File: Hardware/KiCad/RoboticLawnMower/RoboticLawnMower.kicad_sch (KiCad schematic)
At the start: 7 parts, among them J10 Conn_01x02, J11 Conn_01x02

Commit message: layout update
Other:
- sheet Motor_M2 ports: added ADR_0, ADR_1, MOT_5V_OUT, MOT_ENABLE, MOT_SIGNAL, MOT_VEL, MOT_Z/F (DIR), POW_EN, SCL, SDA, ~{alert}; removed none
- sheet Motor_M3 ports: added ADR_0, ADR_1, MOT_5V_OUT, MOT_ENABLE, MOT_SIGNAL, MOT_VEL, MOT_Z/F (DIR), POW_EN, SCL, SDA, ~{alert}; removed none
- sheet Motor_M4 ports: added ADR_0, ADR_1, MOT_5V_OUT, MOT_ENABLE, MOT_SIGNAL, MOT_VEL, MOT_Z/F (DIR), POW_EN, SCL, SDA, ~{alert}; removed none
- sheet Motor_M5 ports: added ADR_0, ADR_1, MOT_5V_OUT, MOT_ENABLE, MOT_SIGNAL, MOT_VEL, MOT_Z/F (DIR), POW_EN, SCL, SDA, ~{alert}; removed none
- sheet i2c_io_pwm ports: added PWM_OUT, SCL, SDA; removed none
- sheet uC ports: added I2C_0_SCL, I2C_0_SDA, MOTOR_CONTROL, SMB_MUX_ADR_0, SMB_MUX_ADR_1, SMB_MUX_ADR_2, UART_0_RXD, UART_0_TXD; removed none

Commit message: schaltplan und layout
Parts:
- added Q1, Q2: BSS123, Package_TO_SOT_SMD:SOT-23, symbol Transistor_FET:BSS123
- added Q3, Q4: Si7141DP, Package_SO:PowerPAK_SO-8_Single, symbol Transistor_FET:Si7141DP
- added R10, R11: 100k, Resistor_SMD:R_0603_1608Metric, symbol Device:R
- added R12, R13: 1K, Resistor_SMD:R_0603_1608Metric, symbol Device:R
- added R6, R7: 100R, Resistor_SMD:R_0603_1608Metric, symbol Device:R
- added R8, R9: 1M, Resistor_SMD:R_0603_1608Metric, symbol Device:R
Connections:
- net Motor_M1/UBATT: now also Q4.5 (D); no longer J11.1 (Pin_1)
- net GNDPWR renamed GND
- net GND: now also Q1.2 (S), Q2.2 (S), R8.2, R9.2
- new net: Q2.1 (G), R7.2, R9.1
- new net: Q4.4 (G), R11.2, R13.2
- new net: Q2.3 (D), R13.1
- new net: Q3.4 (G), R10.2, R12.2
- new net: Q1.1 (G), R6.2, R8.1
- new net: Q1.3 (D), R12.1
- new net +BATT: J11.1 (Pin_1), Q3.1 (S), Q3.2 (S), Q3.3 (S), Q4.1 (S), Q4.2 (S), Q4.3 (S), R10.1, R11.1
- new net Motor_M1..4_EN: R7.1
- new net Motor_M5/UBATT: Q3.5 (D)
- new net Motor_M5_EN: R6.1
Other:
- sheet Motor_M1 ports: added none; removed POW_EN
- sheet Motor_M2 ports: added none; removed POW_EN
- sheet Motor_M3 ports: added none; removed POW_EN
- sheet Motor_M4 ports: added none; removed POW_EN
- sheet Motor_M5 ports: added none; removed POW_EN
- sheet i2c_io_pwm ports: added ~{PCA_9685_OE}; removed none
- sheet uC ports: added I2C_1_SCL, I2C_1_SDA, Motor_M1..4_EN, Motor_M5_EN, ~{PCA_9685_OE}; removed none

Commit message: Layout
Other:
- sheet i2c_smb_mux ports: added none; removed ADR_0, ADR_1, ADR_2
- sheet uC ports: added ~{SMB_MUX_RESET}; removed SMB_MUX_ADR_0, SMB_MUX_ADR_1, SMB_MUX_ADR_2
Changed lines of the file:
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@@
-    (stroke (width 0) (type default) (color 0 0 0 0))
-  )
-  (wire (pts (xy 129.54 184.15) (xy 129.54 101.6))
     (stroke (width 0) (type default) (color 0 0 0 0))
   )
@@
     (stroke (width 0) (type default) (color 0 0 0 0))
   )
+  (wire (pts (xy 139.7 196.85) (xy 130.81 196.85))
+    (stroke (width 0) (type default) (color 0 0 0 0))
+  )
   (bus (pts (xy 280.67 57.15) (xy 280.67 99.06))
     (stroke (width 0) (type default) (color 0 0 0 0))
@@
     (stroke (width 0) (type default) (color 0 0 0 0))
   )
+  (wire (pts (xy 130.81 104.14) (xy 139.7 104.14))
+    (stroke (width 0) (type default) (color 0 0 0 0))
+  )
   (wire (pts (xy 308.61 140.97) (xy 330.2 140.97))
     (stroke (width 0) (type default) (color 0 0 0 0))
@@
     (stroke (width 0) (type default) (color 0 0 0 0))
   )
-  (wire (pts (xy 129.54 101.6) (xy 139.7 101.6))
-    (stroke (width 0) (type default) (color 0 0 0 0))
-  )
   (wire (pts (xy 191.77 109.22) (xy 313.69 109.22))
     (stroke (width 0) (type default) (color 0 0 0 0))
@@
     (stroke (width 0) (type default) (color 0 0 0 0))
   )
-  (wire (pts (xy 130.81 104.14) (xy 130.81 181.61))
-    (stroke (width 0) (type default) (color 0 0 0 0))
-  )
   (wire (pts (xy 313.69 127) (xy 313.69 132.08))
     (stroke (width 0) (type default) (color 0 0 0 0))
@@
     (stroke (width 0) (type default) (color 0 0 0 0))
   )
-  (wire (pts (xy 128.27 186.69) (xy 139.7 186.69))
-    (stroke (width 0) (type default) (color 0 0 0 0))
-  )
   (wire (pts (xy 227.33 36.83) (xy 232.41 36.83))
     (stroke (width 0) (type default) (color 0 0 0 0))
@@
     (stroke (width 0) (type default) (color 0 0 0 0))
   )
+  (wire (pts (xy 130.81 196.85) (xy 130.81 104.14))
+    (stroke (width 0) (type default) (color 0 0 0 0))
+  )
   (wire (pts (xy 232.41 45.72) (xy 232.41 48.26))
     (stroke (width 0) (type default) (color 0 0 0 0))
@@
     (stroke (width 0) (type default) (color 0 0 0 0))
   )
-  (wire (pts (xy 139.7 104.14) (xy 130.81 104.14))
-    (stroke (width 0) (type default) (color 0 0 0 0))
-  )
   (wire (pts (xy 237.49 27.94) (xy 316.23 27.94))
     (stroke (width 0) (type default) (color 0 0 0 0))
@@
     (stroke (width 0) (type default) (color 0 0 0 0))
   )
-  (wire (pts (xy 130.81 181.61) (xy 139.7 181.61))
-    (stroke (width 0) (type default) (color 0 0 0 0))
-  )
   (wire (pts (xy 191.77 109.22) (xy 177.8 109.22))
     (stroke (width 0) (type default) (color 0 0 0 0))
@@
     (stroke (width 0) (type default) (color 0 0 0 0))
   )
-  (wire (pts (xy 139.7 99.06) (xy 128.27 99.06))
-    (stroke (width 0) (type default) (color 0 0 0 0))
-  )
   (wire (pts (xy 316.23 73.66) (xy 330.2 73.66))
     (stroke (width 0) (type default) (color 0 0 0 0))
@@
     (stroke (width 0) (type default) (color 0 0 0 0))
   )
-  (wire (pts (xy 128.27 99.06) (xy 128.27 186.69))
-    (stroke (width 0) (type default) (color 0 0 0 0))
-  )
   (wire (pts (xy 33.02 27.94) (xy 132.08 27.94))
     (stroke (width 0) (type default) (color 0 0 0 0))
@@
   )
   (wire (pts (xy 139.7 106.68) (xy 132.08 106.68))
-    (stroke (width 0) (type default) (color 0 0 0 0))
-  )
-  (wire (pts (xy 139.7 184.15) (xy 129.54 184.15))
     (stroke (width 0) (type default) (color 0 0 0 0))
   )
@@
       (effects (font (size 1.27 1.27)) (justify left))
     )
-    (pin "ADR_2" bidirectional (at 139.7 186.69 180)
-      (effects (font (size 1.27 1.27)) (justify left))
-    )
-    (pin "ADR_1" bidirectional (at 139.7 184.15 180)
-      (effects (font (size 1.27 1.27)) (justify left))
-    )
-    (pin "ADR_0" bidirectional (at 139.7 181.61 180)
-      (effects (font (size 1.27 1.27)) (justify left))
-    )
   )
   (sheet (at 139.7 88.9) (size 38.1 34.29) (fields_autoplaced)
@@
       (effects (font (size 1.27 1.27)) (justify right))
     )
-    (pin "SMB_MUX_ADR_0" bidirectional (at 139.7 104.14 180)
-      (effects (font (size 1.27 1.27)) (justify left))
-    )
-    (pin "SMB_MUX_ADR_1" bidirectional (at 139.7 101.6 180)
-      (effects (font (size 1.27 1.27)) (justify left))
-    )
-    (pin "SMB_MUX_ADR_2" bidirectional (at 139.7 99.06 180)
-      (effects (font (size 1.27 1.27)) (justify left))
-    )
     (pin "~{PCA_9685_OE}" bidirectional (at 177.8 111.76 0)
       (effects (font (size 1.27 1.27)) (justify right))
@@
     (pin "Motor_M5_EN" bidirectional (at 177.8 118.11 0)
       (effects (font (size 1.27 1.27)) (justify right))
+    )
+    (pin "~{SMB_MUX_RESET}" output (at 139.7 104.14 180)
+      (effects (font (size 1.27 1.27)) (justify left))
     )
   )
@@
       (reference "#PWR064") (unit 1) (value "GNDPWR") (footprint "")
     )
+    (path "/611b545d-604c-4bc1-9e50-b1bbed73205e/6ccedec2-da8e-43d4-a940-72a2030bb81b"
+      (reference "#PWR065") (unit 1) (value "+3.3V") (footprint "")
+    )
+    (path "/611b545d-604c-4bc1-9e50-b1bbed73205e/73a8e649-7fe1-4289-b359-82acac05554e"
+      (reference "#PWR066") (unit 1) (value "+3.3V") (footprint "")
+    )
+    (path "/611b545d-604c-4bc1-9e50-b1bbed73205e/d185b2e9-423d-4aa1-ad92-12e9b05fa5c3"
+      (reference "#PWR067") (unit 1) (value "GND") (footprint "")
+    )
+    (path "/611b545d-604c-4bc1-9e50-b1bbed73205e/7f40b2b2-bc40-4156-ae23-f353301d7bda"
+      (reference "#PWR068") (unit 1) (value "+3.3V") (footprint "")
+    )
+    (path "/611b545d-604c-4bc1-9e50-b1bbed73205e/323a30e9-9ec8-4d2c-8720-603c8cc6abc7"
+      (reference "#PWR069") (unit 1) (value "GND") (footprint "")
+    )
+    (path "/6306c3d8-4421-4900-a194-54ab6eebd899/eb218c4a-91a1-4e57-be43-77887926051b"
+      (reference "#PWR070") (unit 1) (value "+3.3V") (footprint "")
+    )
+    (path "/611b545d-604c-4bc1-9e50-b1bbed73205e/ea316622-f00e-479e-9b9d-83cf1784feae"
+      (reference "#PWR071") (unit 1) (value "GND") (footprint "")
+    )
     (path "/39f2b0f3-d323-43fa-8206-419714f3fe7e/66bb9d1c-8659-457d-8200-a79fe0b5ccf5"
       (reference "#PWR0101") (unit 1) (value "GNDPWR") (footprint "")
@@
       (reference "R18") (unit 1) (value "2k2") (footprint "Resistor_SMD:R_0603_1608Metric")
     )
+    (path "/611b545d-604c-4bc1-9e50-b1bbed73205e/c1ac4d05-24d2-49d1-8fd0-958c728ec42a"
+      (reference "R19") (unit 1) (value "10K") (footprint "Resistor_SMD:R_0603_1608Metric")
+    )
+    (path "/611b545d-604c-4bc1-9e50-b1bbed73205e/027d4156-3f39-45ed-96c2-fe0935c5f1bc"
+      (reference "R20") (unit 1) (value "4k7") (footprint "Resistor_SMD:R_0603_1608Metric")
+    )
+    (path "/611b545d-604c-4bc1-9e50-b1bbed73205e/743aa81b-70e2-49b2-bab9-699a75eb9c80"
+      (reference "R21") (unit 1) (value "4k7") (footprint "Resistor_SMD:R_0603_1608Metric")
+    )
+    (path "/611b545d-604c-4bc1-9e50-b1bbed73205e/ff0bdb24-c68e-4ec9-b109-7947acf76e94"
+      (reference "R22") (unit 1) (value "4k7") (footprint "Resistor_SMD:R_0603_1608Metric")
+    )
+    (path "/611b545d-604c-4bc1-9e50-b1bbed73205e/9db69c11-f599-4a53-a000-50c2575872b2"
+      (reference "R23") (unit 1) (value "4k7") (footprint "Resistor_SMD:R_0603_1608Metric")
+    )
+    (path "/611b545d-604c-4bc1-9e50-b1bbed73205e/09da38a8-d19a-4f3c-90fe-6754e1f1f7f9"
+      (reference "R24") (unit 1) (value "4k7") (footprint "Resistor_SMD:R_0603_1608Metric")
+    )
+    (path "/611b545d-604c-4bc1-9e50-b1bbed73205e/a5c8077b-77d1-402b-99fa-59909bf0cffc"
+      (reference "R25") (unit 1) (value "4k7") (footprint "Resistor_SMD:R_0603_1608Metric")
+    )
     (path "/6306c3d8-4421-4900-a194-54ab6eebd899/78684c19-73bc-4253-8b81-9d4a6248cd2f"
       (reference "R26") (unit 1) (value "47K") (footprint "Resistor_SMD:R_0603_1608Metric")
@@
       (reference "R34") (unit 1) (value "N.P.") (footprint "Resistor_SMD:R_0402_1005Metric")
     )
+    (path "/611b545d-604c-4bc1-9e50-b1bbed73205e/8a03f295-4280-476c-a74d-73323f1aa23f"
+      (reference "R35") (unit 1) (value "4k7") (footprint "Resistor_SMD:R_0603_1608Metric")
+    )
+    (path "/611b545d-604c-4bc1-9e50-b1bbed73205e/7a09fee4-0e7b-4f35-b6c2-12bd7c112439"
+      (reference "R36") (unit 1) (value "4k7") (footprint "Resistor_SMD:R_0603_1608Metric")
+    )
+    (path "/611b545d-604c-4bc1-9e50-b1bbed73205e/30251252-206f-466f-a3f4-f51e314c58c9"
+      (reference "R37") (unit 1) (value "10K") (footprint "Resistor_SMD:R_0402_1005Metric")
+    )
+    (path "/611b545d-604c-4bc1-9e50-b1bbed73205e/774526b0-09d1-48c8-9e8d-29d0938edfdc"
+      (reference "R38") (unit 1) (value "N.P.") (footprint "Resistor_SMD:R_0402_1005Metric")
+    )
+    (path "/611b545d-604c-4bc1-9e50-b1bbed73205e/0d107a27-ca60-43be-8cef-bd52e5e4e4ef"
+      (reference "R39") (unit 1) (value "10K") (footprint "Resistor_SMD:R_0402_1005Metric")
+    )
+    (path "/611b545d-604c-4bc1-9e50-b1bbed73205e/c2b299e8-c23b-47ee-b08e-a48be056f621"
+      (reference "R40") (unit 1) (value "N.P.") (footprint "Resistor_SMD:R_0402_1005Metric")
+    )
+    (path "/6306c3d8-4421-4900-a194-54ab6eebd899/4a634291-adde-4b7c-9e83-9b3ebd29c2f5"
+      (reference "R41") (unit 1) (value "4k7") (footprint "Resistor_SMD:R_0603_1608Metric")
+    )
+    (path "/6306c3d8-4421-4900-a194-54ab6eebd899/12d79ae8-cba0-4cfc-91e7-4f626e0342c8"
+      (reference "R42") (unit 1) (value "4k7") (footprint "Resistor_SMD:R_0603_1608Metric")
+    )
     (path "/39f2b0f3-d323-43fa-8206-419714f3fe7e/e02631f0-f8c8-4738-b68d-6c574a73846f"

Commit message: Layout
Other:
- sheet Motor_M1 ports: added none; removed ~{alert}
- sheet Motor_M2 ports: added none; removed ~{alert}
- sheet Motor_M3 ports: added none; removed ~{alert}
- sheet Motor_M4 ports: added none; removed ~{alert}
- sheet Motor_M5 ports: added none; removed ~{alert}
- sheet WLAN ports: added UART_RxD_uC, UART_TxD_uC; removed none
- sheet uC ports: added none; removed MOTOR_CONTROL

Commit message: LAYOUT
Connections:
- net +BATT: now also J10.1 (Pin_1)
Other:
- sheet uC ports: added MOTOR_CTR_CTN_0, MOTOR_CTR_CTN_1, MOTOR_CTR_CTN_2, MOTOR_CTR_CTN_3, MOTOR_CTR_CTN_4; removed none

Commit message: bild hinzugefügt.
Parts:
- added J16: Conn_01x06, Connector_PinHeader_2.54mm:PinHeader_1x06_P2.54mm_Vertical, symbol Connector_Generic:Conn_01x06
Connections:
- net +3.3V: now also J16.1 (Pin_1)
- net GND: now also J16.6 (Pin_6)
- new net uC/UART_0_RXD: J16.3 (Pin_3)
- new net uC/UART_0_TXD: J16.2 (Pin_2)
- new net uC/UART_0_XCK: J16.4 (Pin_4)
- new net uC/UART_0_XDIR: J16.5 (Pin_5)
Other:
- removed sheet WLAN
- sheet uC ports: added UART_0_XCK, UART_0_XDIR; removed none

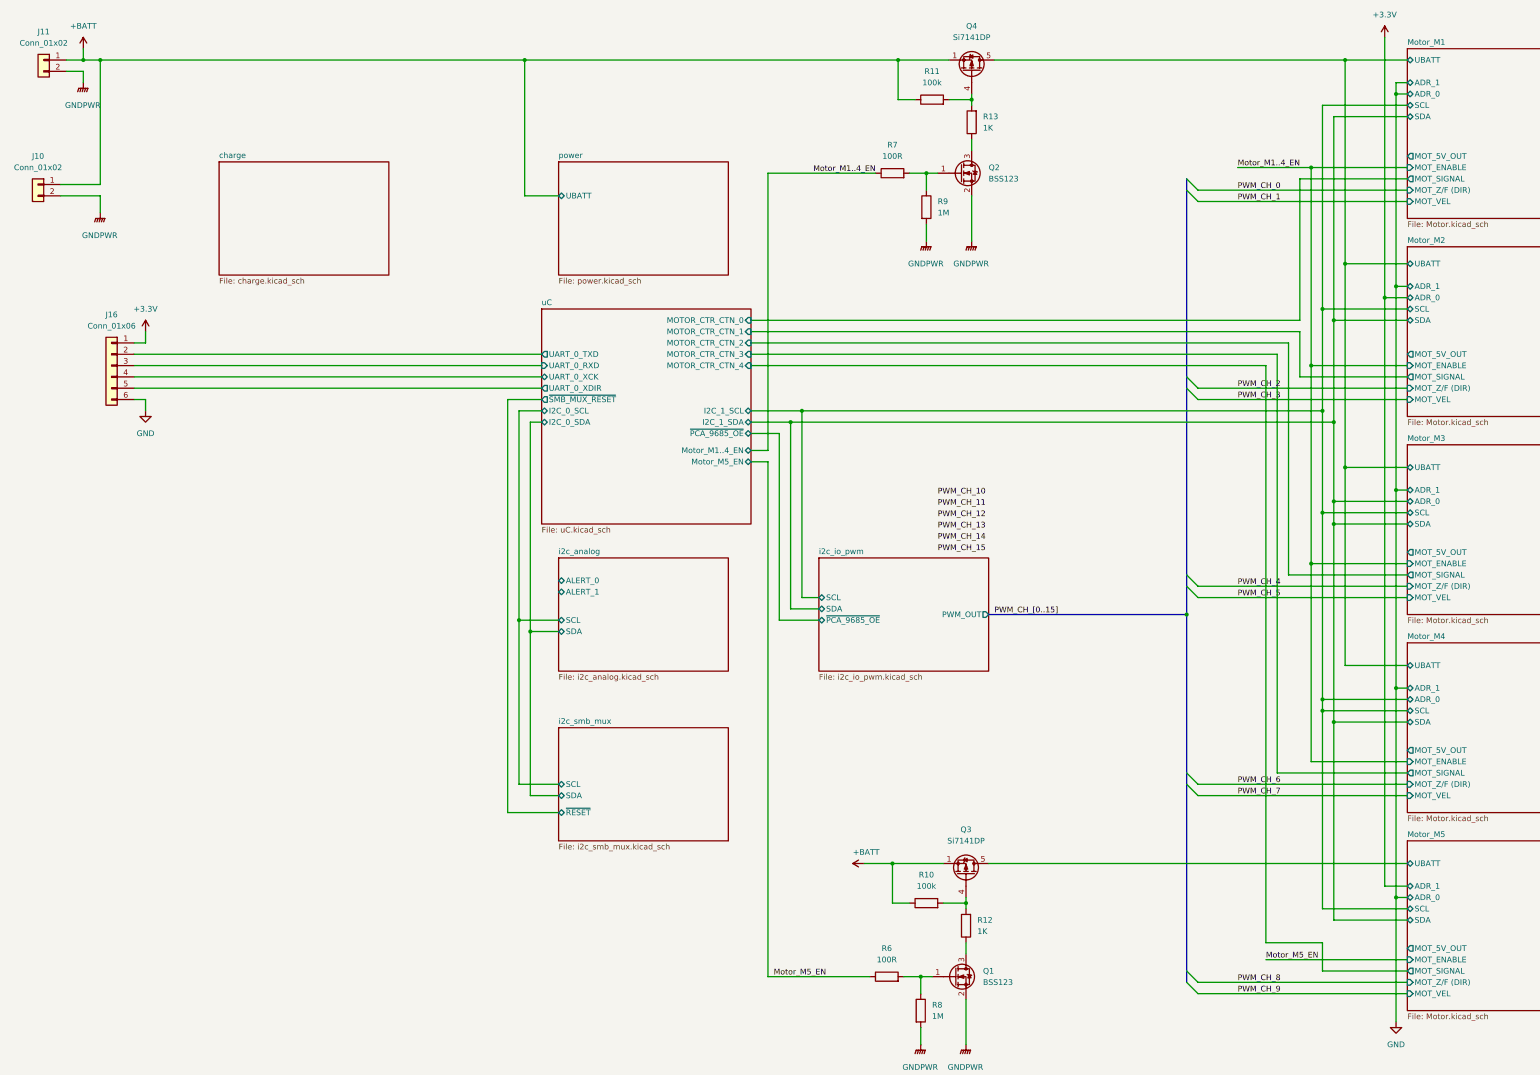
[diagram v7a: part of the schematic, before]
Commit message: Schaltplan und Layout änderung
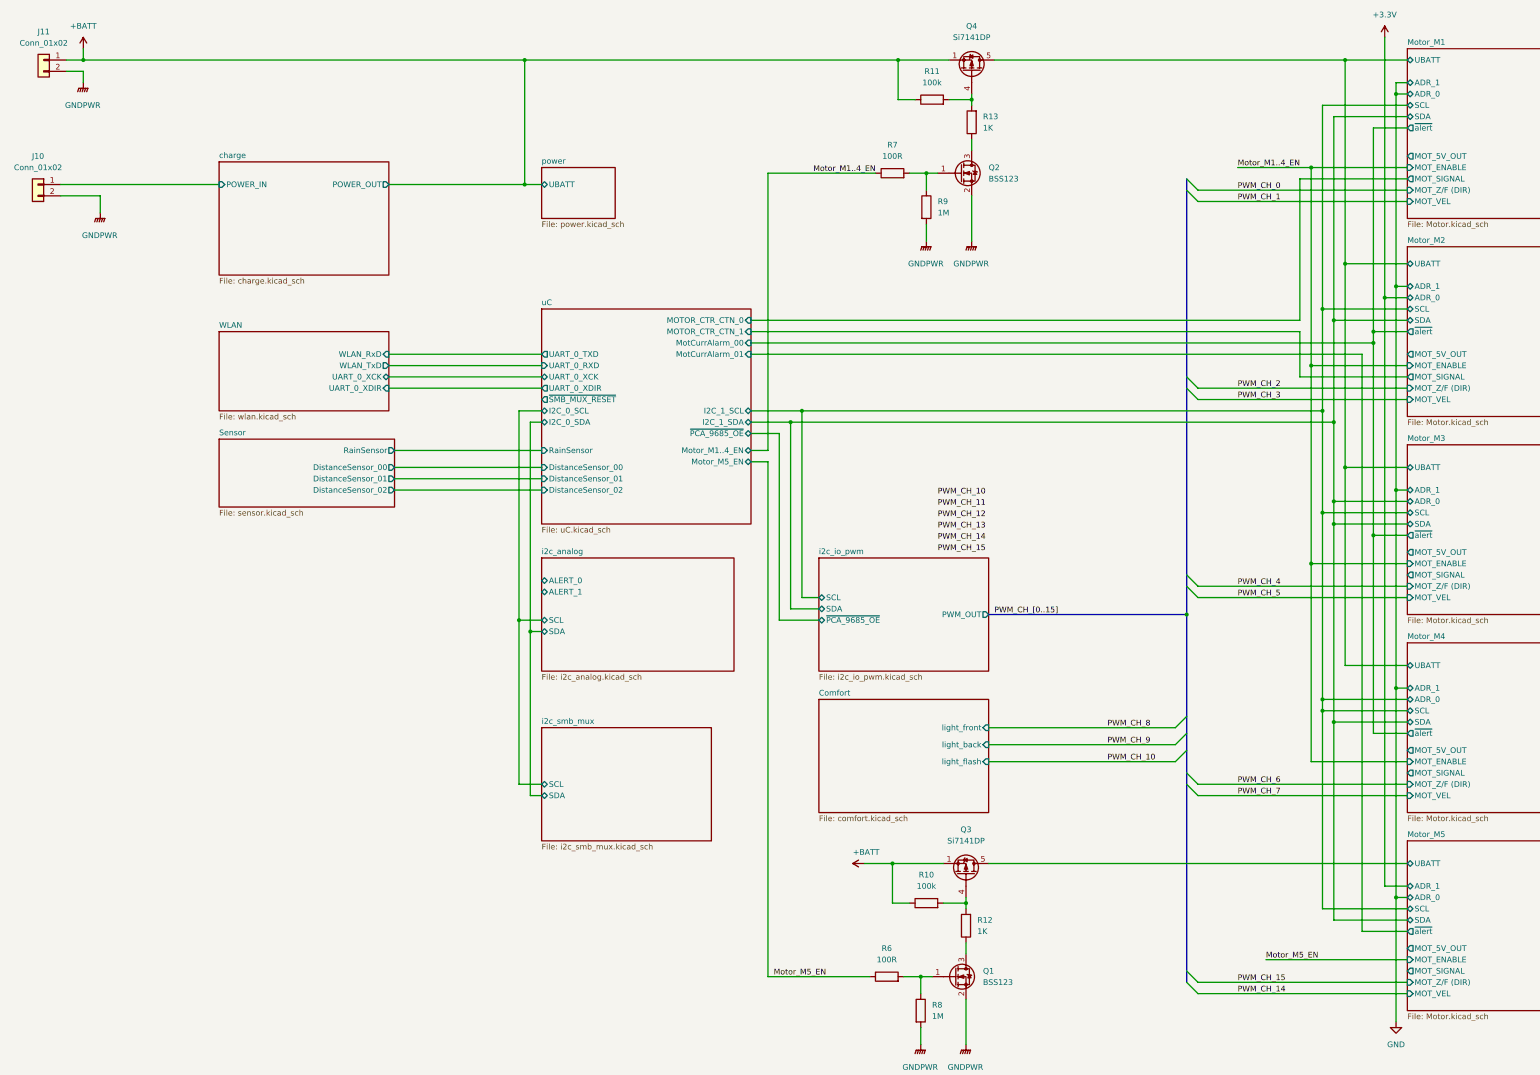
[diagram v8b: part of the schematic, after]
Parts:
- removed J16: Conn_01x06, Connector_PinHeader_2.54mm:PinHeader_1x06_P2.54mm_Vertical, symbol Connector_Generic:Conn_01x06
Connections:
- net +BATT: no longer J10.1 (Pin_1)
- new net charge/POWER_IN: J10.1 (Pin_1)
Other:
- added sheet Comfort (comfort.kicad_sch)
- added sheet Sensor (sensor.kicad_sch)
- added sheet WLAN (wlan.kicad_sch)
- sheet Motor_M1 ports: added ~{alert}; removed none
- sheet Motor_M2 ports: added ~{alert}; removed none
- sheet Motor_M3 ports: added ~{alert}; removed none
- sheet Motor_M4 ports: added ~{alert}; removed none
- sheet Motor_M5 ports: added ~{alert}; removed none
- sheet charge ports: added POWER_IN, POWER_OUT; removed none
- sheet i2c_smb_mux ports: added none; removed ~{RESET}
- sheet uC ports: added DistanceSensor_00, DistanceSensor_01, DistanceSensor_02, MotCurrAlarm_00, MotCurrAlarm_01, RainSensor; removed MOTOR_CTR_CTN_2, MOTOR_CTR_CTN_3, MOTOR_CTR_CTN_4
